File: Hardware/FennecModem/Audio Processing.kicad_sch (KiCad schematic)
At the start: 6 parts

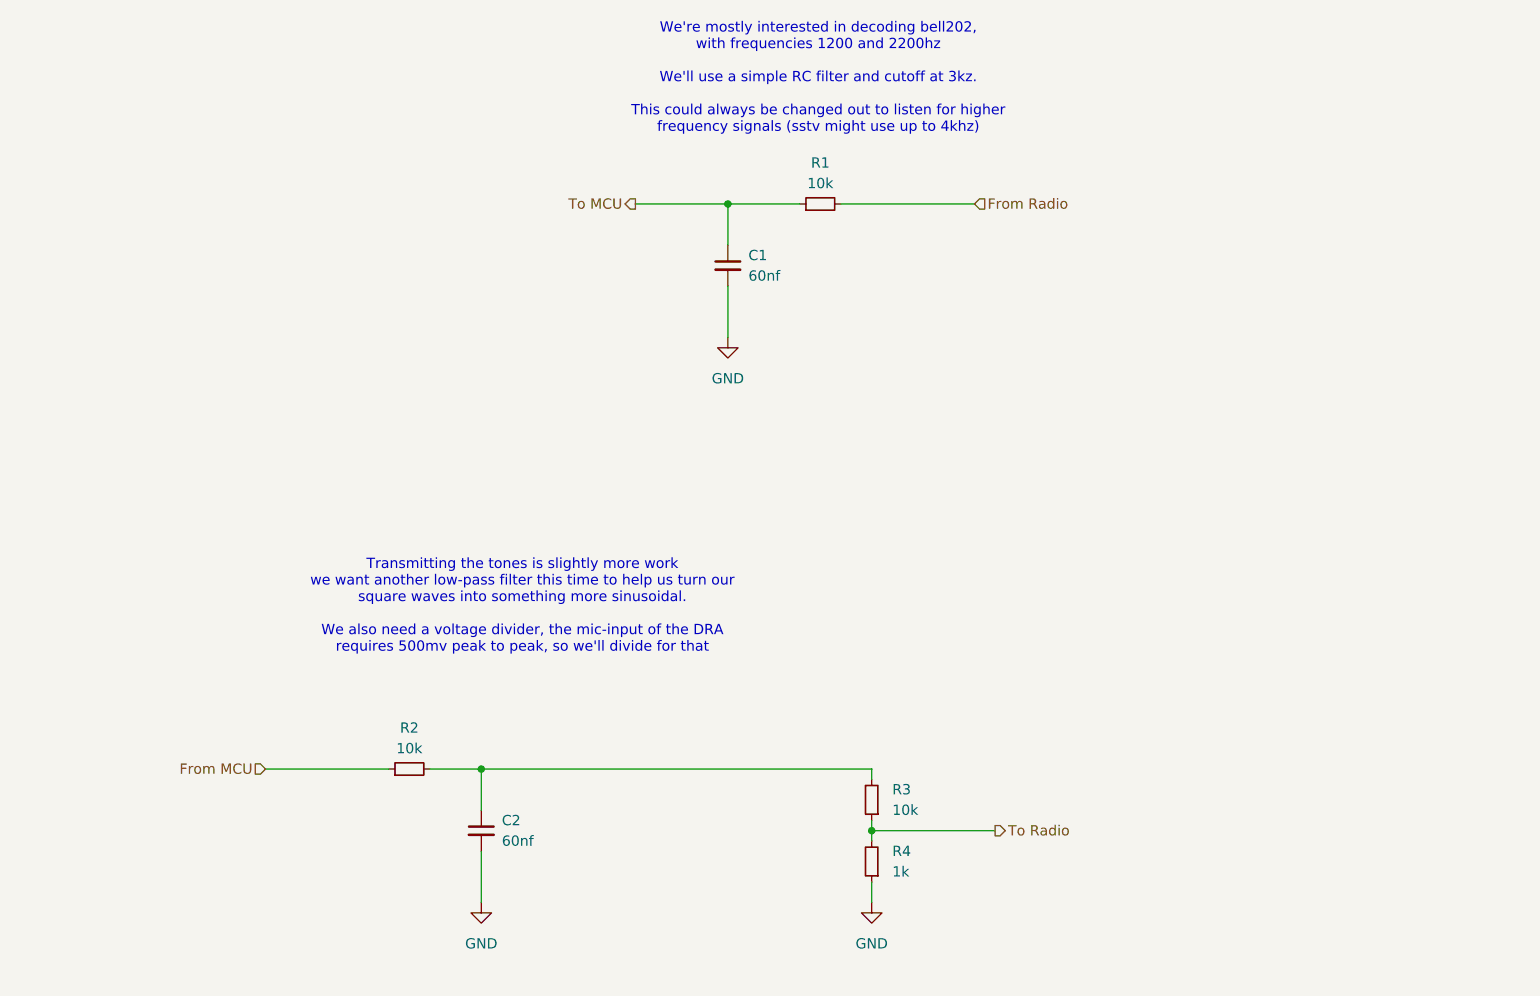
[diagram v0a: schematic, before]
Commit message: Include inital sim and design changes
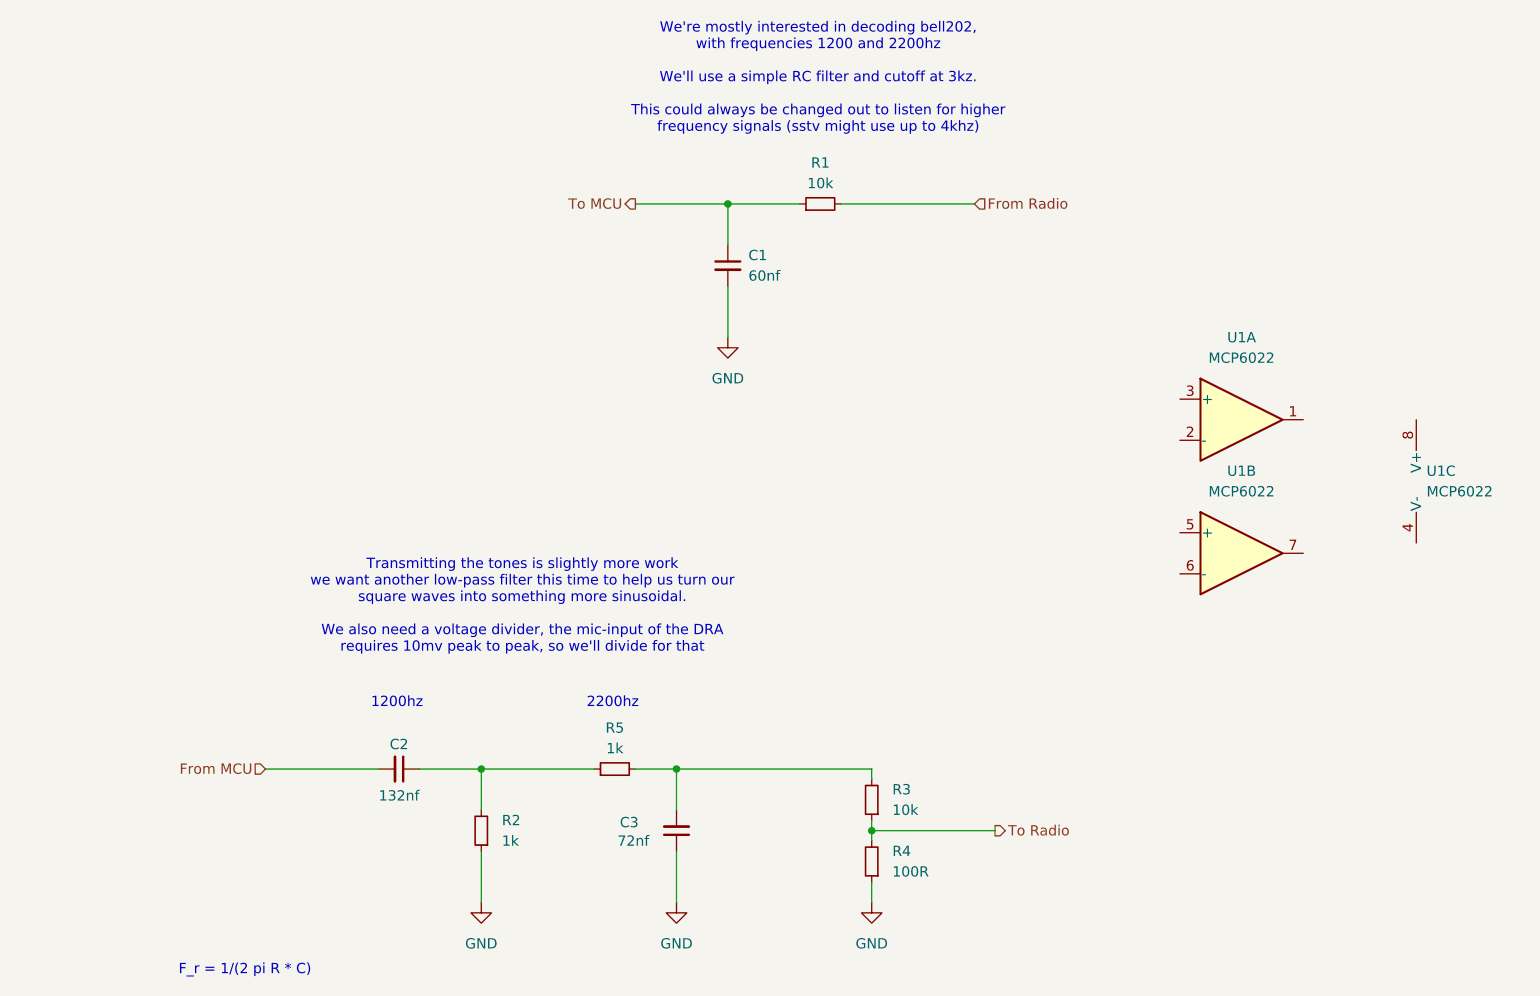
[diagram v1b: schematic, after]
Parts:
- added C3: 72nf, Capacitor_THT:CP_Radial_D4.0mm_P2.00mm, symbol Device:C_Small
- added R5: 1k, Resistor_THT:R_Axial_DIN0207_L6.3mm_D2.5mm_P10.16mm_Horizontal, symbol Device:R_Small
- added U1: MCP6022, Package_SO:SOIC-8_3.9x4.9mm_P1.27mm, symbol Amplifier_Operational:MCP6022
- C2: value 60nf -> 132nf
- R2: value 10k -> 1k
- R4: value 1k -> 100R
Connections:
- net From MCU: now also C2.2; no longer R2.1
- net GND: now also R2.1, C3.1; no longer C2.2
- net at C2.1, R2.2: now also R5.1; no longer R3.2
- new net: C3.2, R3.2, R5.2
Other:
- note added: "1200hz"
- note added: "2200hz"
- note added: "F_r = 1/(2 pi R * C)"
- note added: "Transmitting the tones is slightly more work we want another low-pass filter this time to help us turn our square waves into something more sinusoidal. We also need a voltage divider, the mic-input of the DRA requires 10mv peak to peak, so we'll divide for that"
- note removed: "Transmitting the tones is slightly more work we want another low-pass filter this time to help us turn our square waves into something more sinusoidal. We also need a voltage divider, the mic-input of the DRA requires 500mv peak to peak, so we'll divide for that"

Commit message: Bump fennec pcb
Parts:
- added C4: 1.6nF, Capacitor_SMD:C_0805_2012Metric, symbol Device:C_Small
- added C5: 1uF, Capacitor_SMD:C_0805_2012Metric, symbol Device:C_Small
- added JP1: Bypass Attenuation, Jumper:SolderJumper-2_P1.3mm_Open_TrianglePad1.0x1.5mm, symbol Jumper:SolderJumper_2_Open
- added R6: 0R, Resistor_SMD:R_0805_2012Metric, symbol Device:R_Small
- added RV701: 10K, Potentiometer_SMD:Potentiometer_Bourns_TC33X_Vertical, symbol Device:R_Potentiometer
- C2: value 132nf -> 1.6nF; footprint Capacitor_THT:CP_Radial_D4.0mm_P2.00mm -> Capacitor_SMD:C_0805_2012Metric
- C3: value 72nf -> 360pF; footprint Capacitor_THT:CP_Radial_D4.0mm_P2.00mm -> Capacitor_SMD:C_0805_2012Metric
- R2: value 1k -> 99.4k; footprint Resistor_THT:R_Axial_DIN0207_L6.3mm_D2.5mm_P10.16mm_Horizontal -> Resistor_SMD:R_0805_2012Metric
- R3: value 10k -> 0R; footprint Resistor_THT:R_Axial_DIN0207_L6.3mm_D2.5mm_P10.16mm_Horizontal -> Resistor_SMD:R_0805_2012Metric
- R4: value 100R -> 151k; footprint Resistor_THT:R_Axial_DIN0207_L6.3mm_D2.5mm_P10.16mm_Horizontal -> Resistor_SMD:R_0805_2012Metric
- R5: value 1k -> 291k; footprint Resistor_THT:R_Axial_DIN0207_L6.3mm_D2.5mm_P10.16mm_Horizontal -> Resistor_SMD:R_0805_2012Metric
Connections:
- net From MCU: now also R2.1; no longer C2.2
- net GND: now also C2.2, C3.2, U1.4 (V-), C5.2, RV701.3; no longer C3.1, R2.1, R4.1
- net To Radio: now also JP1.2 (B), RV701.2; no longer R3.1, R4.2
- net +3.3V: now reaches U1.8 (V+)
- net +3.3V: now also C5.1
- net at C2.1, R2.2: now also U1.3 (+); no longer R5.1
- net at U1.1: now also R3.2, R4.1
- net at U1.2 (-): now also R3.1
- net at U1.5 (+): now also C3.1, R5.2
- net at U1.6 (-): now also R6.1
- net at U1.7: now also C4.2, JP1.1 (A), R6.2, RV701.1
- new net: C4.1, R4.2, R5.1
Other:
- note removed: "1200hz"
- note removed: "2200hz"
- note removed: "F_r = 1/(2 pi R * C)"
- note removed: "Transmitting the tones is slightly more work we want another low-pass filter this time to help us turn our square waves into something more sinusoidal. We also need a voltage divider, the mic-input of the DRA requires 10mv peak to peak, so we'll divide for that"
- moved on the sheet: U1A, U1B

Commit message: Route!
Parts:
- removed C1: 60nf, Capacitor_THT:CP_Radial_D4.0mm_P2.00mm, symbol Device:C_Small
- added C6: 110nf, Capacitor_SMD:C_0805_2012Metric, symbol Device:C_Small
- added R7: 0R, Resistor_SMD:R_0805_2012Metric, symbol Device:R_Small
- added R8: 100k, Resistor_SMD:R_0805_2012Metric, symbol Device:R_Small
- added RV1: 10K, Potentiometer_SMD:Potentiometer_Bourns_TC33X_Vertical, symbol Device:R_Potentiometer
- R1: value 10k -> 100k; footprint Resistor_THT:R_Axial_DIN0207_L6.3mm_D2.5mm_P10.16mm_Horizontal -> Resistor_SMD:R_0805_2012Metric
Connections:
- net +3.3V: now also R1.2
- net From Radio: now also R7.2; no longer R1.2
- net To MCU: now also C6.1, R8.2
- new net: R7.1, RV1.3
- new net: C6.2, RV1.2
- new net GNDA: R8.1, RV1.1
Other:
- note removed: "We're mostly interested in decoding bell202, with frequencies 1200 and 2200hz We'll use a simple RC filter and cutoff at 3kz. This could always be changed out to listen for higher frequency signals (sstv might use up to 4khz)"

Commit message: Add all nets
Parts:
- renumbered JP1 to JPBP1
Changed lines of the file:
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@@
 		(dnp no)
 		(fields_autoplaced yes)
-		(property "Reference" "JP1"
+		(property "Reference" "JPBP1"
 			(at 209.55 107.95 0)
 			(effects
@@
 			(project ""
 				(path "/8cb1f8f8-0f28-4c6f-8a0b-e6b064917aa9/e2ade840-7bcb-4a84-9d53-fd6392ab05ef"
-					(reference "JP1")
+					(reference "JPBP1")
 					(unit 1)
 				)
